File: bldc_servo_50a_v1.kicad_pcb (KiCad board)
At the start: 2 copper layers, 101 parts, among them IC1 DRV8305NQPHPRQ1, J1 CAN_JST-1, J2 CAN_JST-2, J4 Fan_JST, J5 SWD, Q1 BSC010N04LS, Q2 BSC010N04LS, Q3 BSC010N04LS, Q4 BSC010N04LS, Q5 BSC010N04LS, Q6 BSC010N04LS, U1 TLV75533PDBV, U2 SN65HVD230, U3 LMR51430, U4 TPS2051BDBV, U5 STM32G431CBT6

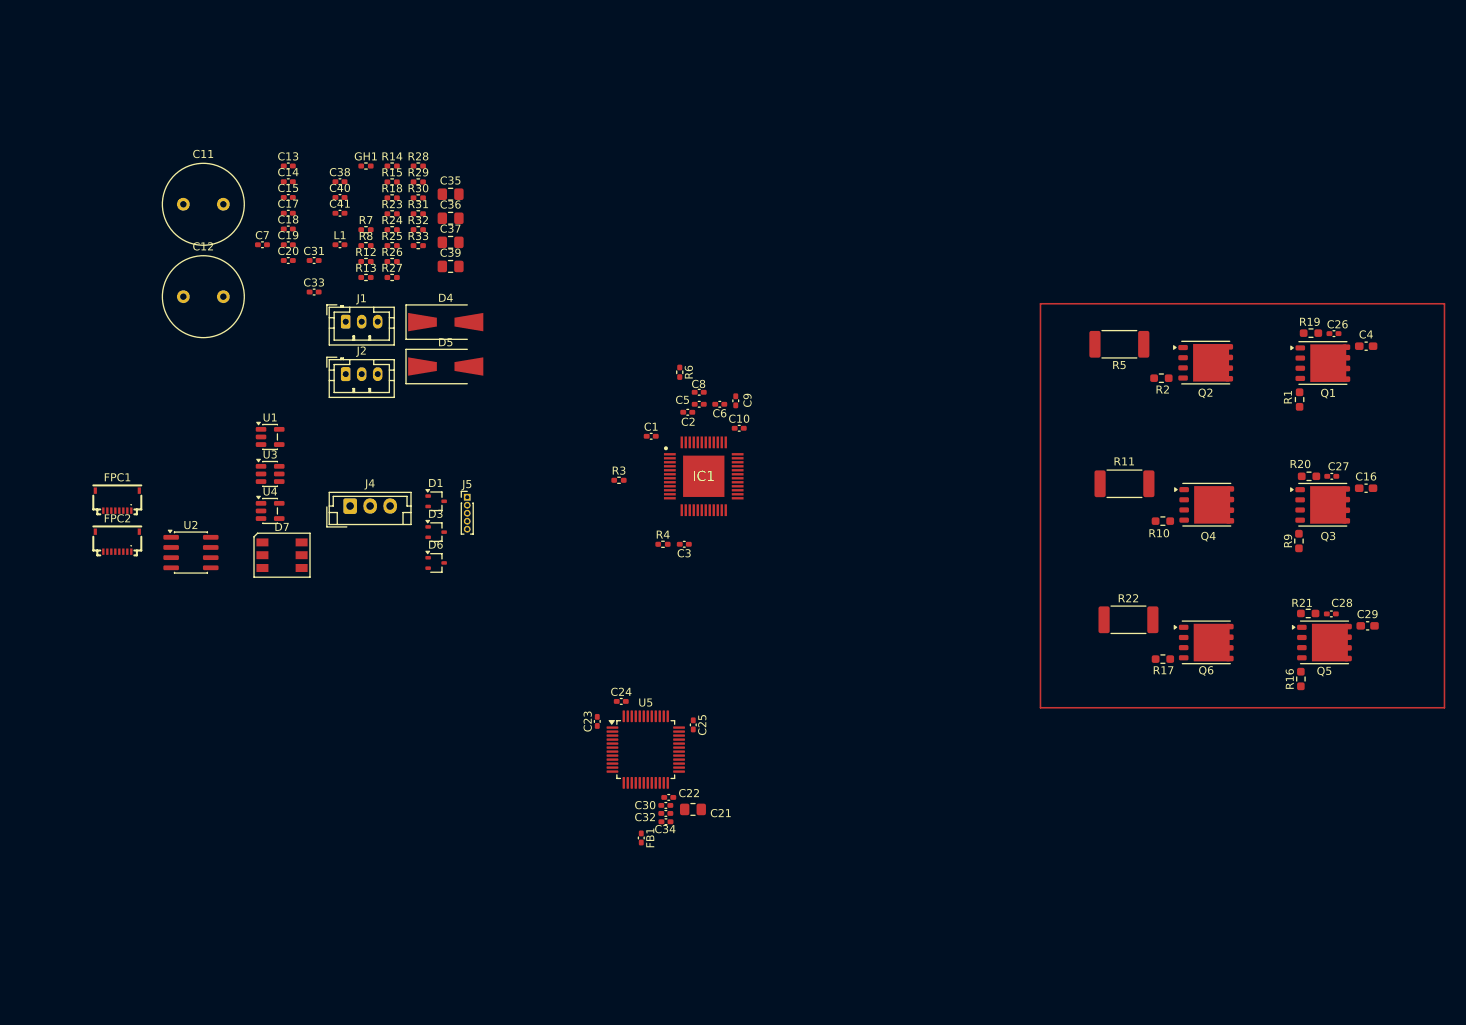
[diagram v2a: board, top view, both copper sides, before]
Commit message: Removed duplicate V_Sensing
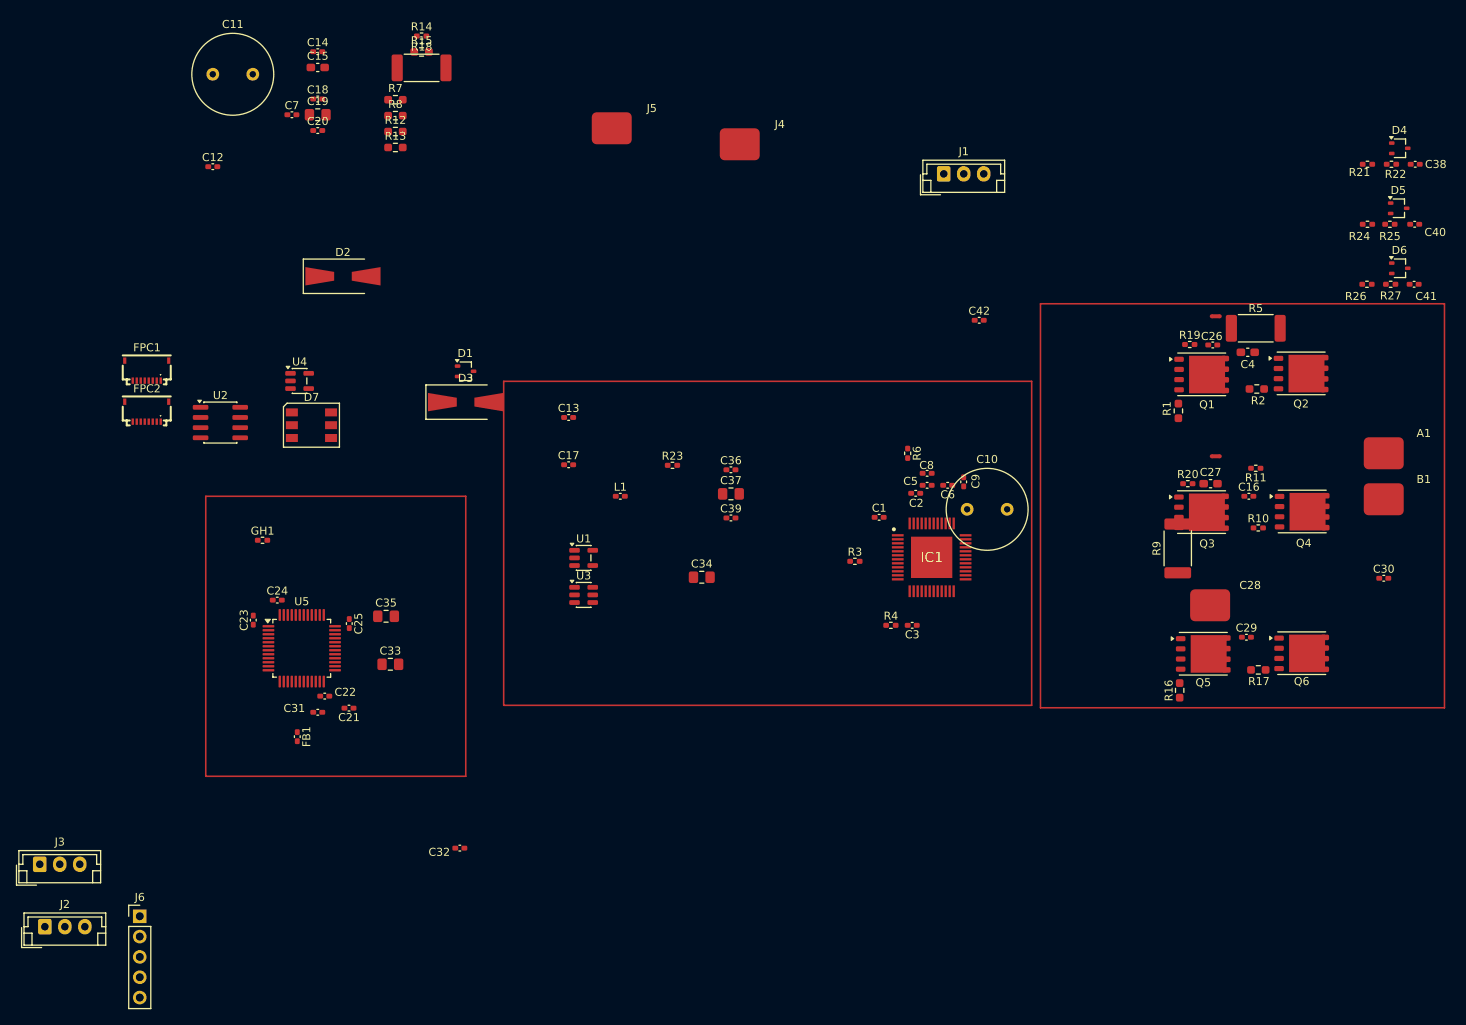
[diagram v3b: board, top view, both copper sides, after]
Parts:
- removed R28, R31, R33: 5k, Resistor_SMD:R_0402_1005Metric_Pad0.72x0.64mm_HandSolder
- removed R29: 10k1, Resistor_SMD:R_0402_1005Metric_Pad0.72x0.64mm_HandSolder
- removed R30, R32: 34.8k, Resistor_SMD:R_0402_1005Metric_Pad0.72x0.64mm_HandSolder
- added A1: A, Solder_Pads:Solder_Pad_5mmx4mm, F.Cu at (224.5, 58.6)
- added B1: B, Solder_Pads:Solder_Pad_5mmx4mm, F.Cu at (224.5, 64.4)
- added C42: 100n, Capacitor_SMD:C_0402_1005Metric_Pad0.74x0.62mm_HandSolder, F.Cu at (173.9, 39.5)
- added D2: SMAJ440A_TVS, Diode_SMD:D_SMA-SMB_Universal_Handsoldering, F.Cu at (94.4, 34.0)
- added J3: Fan_JST, Connector_JST:JST_EH_B3B-EH-A_1x03_P2.50mm_Vertical, F.Cu at (56.5, 107.5)
- added J6: SWD, Connector_PinHeader_2.54mm:PinHeader_1x05_P2.54mm_Vertical, F.Cu at (69.0, 114.0)
- added NT1: NetTie_2, NetTie:NetTie-2_SMD_Pad0.5mm, F.Cu at (203.5, 39.0)
- added NT2: NetTie_2, NetTie:NetTie-2_SMD_Pad0.5mm, F.Cu at (203.5, 56.5)
- added NT3: NetTie_2, NetTie:NetTie-2_SMD_Pad0.5mm, F.Cu at (203.5, 74.5)
- C10: value 1u -> 470u; footprint Capacitor_SMD:C_0402_1005Metric_Pad0.74x0.62mm_HandSolder -> Capacitor_THT:C_Radial_D10.0mm_H16.0mm_P5.00mm
- C12: value 470u -> 1u; footprint Capacitor_THT:C_Radial_D10.0mm_H16.0mm_P5.00mm -> Capacitor_SMD:C_0402_1005Metric_Pad0.74x0.62mm_HandSolder
- C13: value 1u -> 0.1u
- C14: value 0.1u -> 0.01u
- C15: value 0.01u -> 1u; footprint Capacitor_SMD:C_0402_1005Metric_Pad0.74x0.62mm_HandSolder -> Capacitor_SMD:C_0603_1608Metric_Pad1.08x0.95mm_HandSolder
- C16: footprint Capacitor_SMD:C_0603_1608Metric_Pad1.08x0.95mm_HandSolder -> Capacitor_SMD:C_0402_1005Metric_Pad0.74x0.62mm_HandSolder
- C18, C31, C32: value 1u -> 100n
- C19: value 1u -> 10u; footprint Capacitor_SMD:C_0402_1005Metric_Pad0.74x0.62mm_HandSolder -> Capacitor_SMD:C_0805_2012Metric_Pad1.18x1.45mm_HandSolder
- C21, C36, C39: value 10u -> 100n; footprint Capacitor_SMD:C_0805_2012Metric_Pad1.18x1.45mm_HandSolder -> Capacitor_SMD:C_0402_1005Metric_Pad0.74x0.62mm_HandSolder
- C24, C25: value 100n -> 22n
- C27: value 22n -> 1u; footprint Capacitor_SMD:C_0402_1005Metric_Pad0.74x0.62mm_HandSolder -> Capacitor_SMD:C_0603_1608Metric_Pad1.08x0.95mm_HandSolder
- C28: value 22n -> C; footprint Capacitor_SMD:C_0402_1005Metric_Pad0.74x0.62mm_HandSolder -> Solder_Pads:Solder_Pad_5mmx4mm
- C29: value 1u -> 10n; footprint Capacitor_SMD:C_0603_1608Metric_Pad1.08x0.95mm_HandSolder -> Capacitor_SMD:C_0402_1005Metric_Pad0.74x0.62mm_HandSolder
- C30: value 10n -> 1u
- C33, C34: value 100n -> 10u; footprint Capacitor_SMD:C_0402_1005Metric_Pad0.74x0.62mm_HandSolder -> Capacitor_SMD:C_0805_2012Metric_Pad1.18x1.45mm_HandSolder
- C38, C40, C41: value 100n -> 1u
- C7: value 1u -> 4.7u
- C8: value 4.7u -> 2.2u
- C9: value 2.2u -> 1u
- D1: value BAT54SW -> D_Schottky
- D3: value BAT54SW -> SMAJ440A_TVS; footprint Package_TO_SOT_SMD:SOT-323_SC-70 -> Diode_SMD:D_SMA-SMB_Universal_Handsoldering
- D4, D5: value SMAJ440A_TVS -> BAT54SW; footprint Diode_SMD:D_SMA-SMB_Universal_Handsoldering -> Package_TO_SOT_SMD:SOT-323_SC-70
- J1, J2: footprint Connector_JST:JST_PH_B3B-PH-K_1x03_P2.00mm_Vertical -> Connector_JST:JST_EH_B3B-EH-A_1x03_P2.50mm_Vertical
- J4: value Fan_JST -> PVDD; footprint Connector_JST:JST_EH_B3B-EH-A_1x03_P2.50mm_Vertical -> Solder_Pads:Solder_Pad_5mmx4mm
- J5: value SWD -> GND; footprint Connector_PinHeader_1.00mm:PinHeader_1x05_P1.00mm_Vertical -> Solder_Pads:Solder_Pad_5mmx4mm
- R10, R21: value 10 -> 34.8k; footprint Resistor_SMD:R_0603_1608Metric_Pad0.98x0.95mm_HandSolder -> Resistor_SMD:R_0402_1005Metric_Pad0.72x0.64mm_HandSolder
- R11, R22: value 1m -> 5k; footprint Resistor_SMD:R_2512_6332Metric_Pad1.40x3.35mm_HandSolder -> Resistor_SMD:R_0402_1005Metric_Pad0.72x0.64mm_HandSolder
- R12, R7: value 34.8k -> 10; footprint Resistor_SMD:R_0402_1005Metric_Pad0.72x0.64mm_HandSolder -> Resistor_SMD:R_0603_1608Metric_Pad0.98x0.95mm_HandSolder
- R13, R15, R8: value 5k -> 10; footprint Resistor_SMD:R_0402_1005Metric_Pad0.72x0.64mm_HandSolder -> Resistor_SMD:R_0603_1608Metric_Pad0.98x0.95mm_HandSolder
- R14: value 34.8k -> 120
- R18: value 120 -> 1m; footprint Resistor_SMD:R_0402_1005Metric_Pad0.72x0.64mm_HandSolder -> Resistor_SMD:R_2512_6332Metric_Pad1.40x3.35mm_HandSolder
- R19: value 10 -> 100k; footprint Resistor_SMD:R_0603_1608Metric_Pad0.98x0.95mm_HandSolder -> Resistor_SMD:R_0402_1005Metric_Pad0.72x0.64mm_HandSolder
- R20: value 10 -> 13.7k; footprint Resistor_SMD:R_0603_1608Metric_Pad0.98x0.95mm_HandSolder -> Resistor_SMD:R_0402_1005Metric_Pad0.72x0.64mm_HandSolder
- R23: value 100k -> 10k1
- R24: value 13.7k -> 34.8k
- R25, R27: value 34.8k -> 5k
- R26: value 5k -> 34.8k
- R9: value 10 -> 1m; footprint Resistor_SMD:R_0603_1608Metric_Pad0.98x0.95mm_HandSolder -> Resistor_SMD:R_2512_6332Metric_Pad1.40x3.35mm_HandSolder
- moved C41 134.6 mm to (228.3, 35.0)
- moved C38 134.4 mm to (228.4, 20.0)
- moved C40 134.4 mm to (228.4, 27.5)
- moved D6 126.0 mm to (226.5, 33.0)
- moved R27 124.8 mm to (225.4, 35.0)
- moved R25 124.7 mm to (225.3, 27.5)
- moved R24 121.9 mm to (222.5, 27.5)
- moved R26 121.9 mm to (222.4, 35.0)
- moved D4 121.2 mm to (226.5, 18.0)
- moved D5 120.8 mm to (226.4, 25.5)
- moved C30 94.1 mm to (224.5, 71.8)
- moved J2 78.6 mm to (57.1, 115.3)
- moved J1 77.0 mm to (169.5, 21.2)
- moved R22 65.7 mm to (225.5, 20.0), turned to 0 degrees
- moved J4 64.8 mm to (144.0, 20.0)
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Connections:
- C10 pad 1: Net-(IC1-VCP_LSD) -> PVDD
- C12 pad 1: PVDD -> +5V
- C12 pad 2: GND -> Net-(U1-GND)
- C13 pad 1: +5V -> PVDD
- C13 pad 2: Net-(U1-GND) -> GND
- C16 pad 1: PVDD -> +3.3V
- C16 pad 2: GND -> Net-(U1-GND)
- C17 pad 1: +3.3V -> /PVDDSENSE
- C17 pad 2: Net-(U1-GND) -> GND
- C18 pad 1: /BSENSE -> +3.3V
- C19 pad 1: /PVDDSENSE -> +3.3V
- C24 pad 1: +3.3V -> /R_C_PhaseA
- C24 pad 2: GND -> PVDD
- C25 pad 1: +3.3V -> /R_C_PhaseB
- C25 pad 2: GND -> PVDD
- C26 pad 1: /R_C_PhaseA -> /R_C_PhaseC
- C27 pad 1: /R_C_PhaseB -> PVDD
- C27 pad 2: PVDD -> GND
- C28 pad 1: /R_C_PhaseC -> /PHASE_C
- C29 pad 1: PVDD -> +3.3VA
- C31 pad 1: /CSENSE -> /5V_SW
- C31 pad 2: GND -> /5V_BOOT
- C33 pad 1: /5V_SW -> +5V
- C33 pad 2: /5V_BOOT -> GND
- C34 pad 1: +3.3VA -> PVDD
- C38 pad 1: PVDD -> Net-(D4-COM)
- C39 pad 1: +5V -> /NRST
- C40 pad 1: /NRST -> Net-(D5-COM)
- C41 pad 1: GND -> Net-(D6-COM)
- C41 pad 2: +5V -> GND
- C7 pad 1: /ASENSE -> PVDD
- C8 pad 1: PVDD -> Net-(IC1-VCPH)
- C8 pad 2: GND -> PVDD
- C9 pad 1: Net-(IC1-VCPH) -> Net-(IC1-VCP_LSD)
- C9 pad 2: PVDD -> GND
- D1 pad 1: GND -> +3.3V
- D1 pad 2: +3V3 -> /PVDDSENSE
- D1 pad 3: /ASENSE -> (no net)
- D3 pad 1: GND -> /CAN_L
- D3 pad 2: +3V3 -> GND
- D4 pad 1: /CAN_H -> GND
- D4 pad 2: GND -> +3V3
- D5 pad 1: /CAN_L -> GND
- D5 pad 2: GND -> +3V3
- D6 pad 3: /CSENSE -> Net-(D6-COM)
- IC1 pad 20: GND -> /SP3
- IC1 pad 22: GND -> /SP2
- IC1 pad 23: /SN1 -> /SL_A
- J4 pad 1: /FAN -> PVDD
- J5 pad 1: +3.3V -> GND
- R10 pad 1: /GL_B -> PVDD
- R10 pad 2: Net-(Q4-G) -> /PVDDSENSE
- R11 pad 1: /SL_B -> /PVDDSENSE
- R12 pad 1: PVDD -> /GH_C
- R12 pad 2: /PVDDSENSE -> Net-(Q5-G)
- R13 pad 1: /PVDDSENSE -> /GL_C
- R13 pad 2: GND -> Net-(Q6-G)
- R14 pad 1: /PHASE_B -> Net-(JP1-A)
- R14 pad 2: /BSENSE -> /CAN_L
- R15 pad 1: /BSENSE -> /PHASE_A
- R15 pad 2: GND -> /R_C_PhaseA
- R16 pad 1: /GH_C -> /PHASE_B
- R16 pad 2: Net-(Q5-G) -> /R_C_PhaseB
- R17 pad 1: /GL_C -> /PHASE_C
- R17 pad 2: Net-(Q6-G) -> /R_C_PhaseC
- R18 pad 1: Net-(JP1-A) -> /SL_C
- R18 pad 2: /CAN_L -> /SP3
- R19 pad 1: /PHASE_A -> +5V
- R19 pad 2: /R_C_PhaseA -> /5V_FB
- R20 pad 1: /PHASE_B -> /5V_FB
- R20 pad 2: /R_C_PhaseB -> GND
- R21 pad 1: /PHASE_C -> /PHASE_A
- R21 pad 2: /R_C_PhaseC -> /SH_A_SENSE
- R22 pad 1: /SL_C -> /SH_A_SENSE
- R23 pad 1: +5V -> +3V3
- R23 pad 2: /5V_FB -> /TEMP
- R24 pad 1: /5V_FB -> /PHASE_B
- R24 pad 2: GND -> /SH_B_SENSE
- R25 pad 1: /PHASE_C -> /SH_B_SENSE
- R25 pad 2: /CSENSE -> GND
- R26 pad 1: /CSENSE -> /PHASE_C
- R26 pad 2: GND -> /SH_C_SENSE
- R27 pad 1: /PHASE_A -> /SH_C_SENSE
- R27 pad 2: /SH_A_SENSE -> GND
- R5 pad 2: GND -> /SP1
- R7 pad 1: /PHASE_A -> /GH_B
- R7 pad 2: /ASENSE -> Net-(Q3-G)
- R8 pad 1: /ASENSE -> /GL_B
- R8 pad 2: GND -> Net-(Q4-G)
- R9 pad 1: /GH_B -> /SL_B
- R9 pad 2: Net-(Q3-G) -> /SP2

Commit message: Structure for PCB, tentative
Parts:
- moved C30 145.9 mm to (82.5, 38.1)
- moved R18 124.6 mm to (208.9, 75.5), turned to 180 degrees
- moved C29 118.7 mm to (93.9, 44.1)
- moved C24 112.5 mm to (194.9, 45.5)
- moved C15 104.0 mm to (191.8, 34.6)
- moved C25 101.0 mm to (195.2, 63.0), turned to 0 degrees
- moved R15 99.5 mm to (194.9, 47.0), turned to 180 degrees
- moved J1 93.9 mm to (90.2, 71.6)
- moved R12 88.8 mm to (187.1, 37.5)
- moved R13 88.8 mm to (187.1, 39.5)
- moved R7 88.8 mm to (187.1, 33.5)
- moved R8 88.8 mm to (187.1, 35.5)
- moved C16 88.1 mm to (122.7, 38.1)
- moved C7 86.5 mm to (168.7, 45.1), turned to 180 degrees
- moved C11 79.6 mm to (156.7, 21.1)
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
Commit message: Wip: before fixing footprints
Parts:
- moved C11 40.5 mm to (173.5, 58.0)
- moved C10 37.9 mm to (184.5, 58.0)
- moved J4 11.9 mm to (166.5, 91.1)
- moved J5 11.9 mm to (173.5, 91.1)
- moved NT3 9.96 mm to (213.0, 71.5), turned to 90 degrees
- moved R17 9.78 mm to (187.9, 76.6)
- moved C26 9.78 mm to (187.7, 75.1)
- moved Q5 9.78 mm to (193.8, 75.8)
- moved FPC1 9.78 mm to (77.0, 90.5), turned to 180 degrees
- moved Q6 9.54 mm to (206.8, 75.1)
- moved R18 7.05 mm to (216.0, 75.5)
- moved C13 6.46 mm to (143.1, 22.0)
- moved C14 6.46 mm to (143.1, 23.0)
- moved C17 6.46 mm to (145.5, 23.0)
- moved D1 6.46 mm to (144.1, 27.5)
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
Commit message: Schematic done
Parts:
- removed A1: A, Solder_Pads:Solder_Pad_5mmx4mm
- removed B1: B, Solder_Pads:Solder_Pad_5mmx4mm
- removed D7: WS2812, LED_SMD:LED_WS2812_PLCC6_5.0x5.0mm_P1.6mm
- removed GH1: 10k, Resistor_SMD:R_0402_1005Metric_Pad0.72x0.64mm_HandSolder
- removed IC1: DRV8305NQPHPRQ1, DRV8305NQPHPRQ1:QFP50P900X900X120-49N
- removed J6: SWD, Connector_PinHeader_2.54mm:PinHeader_1x05_P2.54mm_Vertical
- added C43: 100n, Capacitor_SMD:C_0402_1005Metric_Pad0.74x0.62mm_HandSolder, F.Cu at (156.4, 30.0)
- added C44: 1u, Capacitor_SMD:C_0603_1608Metric_Pad1.08x0.95mm_HandSolder, F.Cu at (115.1, 18.6)
- added C45: 1u, Capacitor_SMD:C_0603_1608Metric_Pad1.08x0.95mm_HandSolder, F.Cu at (115.1, 21.1)
- added C46: 100n, Capacitor_SMD:C_0402_1005Metric_Pad0.74x0.62mm_HandSolder, F.Cu at (85.2, 97.9)
- added C47: 100n, Capacitor_SMD:C_0402_1005Metric_Pad0.74x0.62mm_HandSolder, F.Cu at (162.4, -9.00)
- added C48: 100n, Capacitor_SMD:C_0402_1005Metric_Pad0.74x0.62mm_HandSolder, F.Cu at (50.9, 167.9)
- added C49: 1u, Capacitor_SMD:C_0603_1608Metric_Pad1.08x0.95mm_HandSolder, F.Cu at (43.7, 125.4)
- added C50: 1n, Capacitor_SMD:C_0603_1608Metric_Pad1.08x0.95mm_HandSolder, F.Cu at (226.6, 81.5)
- added C51: 1n, Capacitor_SMD:C_0603_1608Metric_Pad1.08x0.95mm_HandSolder, F.Cu at (243.8, 111.6)
- added C52: 1n, Capacitor_SMD:C_0603_1608Metric_Pad1.08x0.95mm_HandSolder, F.Cu at (269.4, 143.7)
- added C53: 1u, Capacitor_SMD:C_0603_1608Metric_Pad1.08x0.95mm_HandSolder, F.Cu at (73.6, 175.5)
- added C54: 1n, Capacitor_SMD:C_0402_1005Metric_Pad0.74x0.62mm_HandSolder, F.Cu at (229.9, 104.0)
- added C55: 1n, Capacitor_SMD:C_0402_1005Metric_Pad0.74x0.62mm_HandSolder, F.Cu at (255.9, 135.5)
- added C56: 1n, Capacitor_SMD:C_0402_1005Metric_Pad0.74x0.62mm_HandSolder, F.Cu at (281.4, 167.5)
- added H1: ~, positive_altitude:Positive_Altitude_M2_Hole, F.Cu at (167.5, 175.8)
- added H2: ~, positive_altitude:Positive_Altitude_M2_Hole, F.Cu at (167.5, 181.0)
- added H3: ~, positive_altitude:Positive_Altitude_M2_Hole, F.Cu at (167.5, 186.2)
- added JP1: Enable_CAN_Termination_1, Jumper:SolderJumper-2_P1.3mm_Open_RoundedPad1.0x1.5mm, F.Cu at (85.2, 101.4)
- added NT10: NetTie_2, positive_altitude:NetTie-2_SMD_Pad0.2mm, F.Cu at (281.8, 157.0)
- added NT11: NetTie_2, positive_altitude:NetTie-2_SMD_Pad0.2mm, F.Cu at (281.8, 158.5)
- added NT12: NetTie_2, positive_altitude:NetTie-2_SMD_Pad0.2mm, F.Cu at (281.8, 160.0)
- added NT4: NetTie_2, positive_altitude:NetTie-2_SMD_Pad0.2mm, F.Cu at (236.4, 94.0)
- added NT5: NetTie_2, positive_altitude:NetTie-2_SMD_Pad0.2mm, F.Cu at (238.9, 127.6)
- added NT6: NetTie_2, positive_altitude:NetTie-2_SMD_Pad0.2mm, F.Cu at (238.9, 129.1)
- added NT7: NetTie_2, positive_altitude:NetTie-2_SMD_Pad0.2mm, F.Cu at (240.5, 126.1)
- added NT8: NetTie_2, positive_altitude:NetTie-2_SMD_Pad0.2mm, F.Cu at (240.5, 127.6)
- added NT9: NetTie_2, positive_altitude:NetTie-2_SMD_Pad0.2mm, F.Cu at (279.3, 158.5)
- added P1: PVDD, positive_altitude:Soldering_Pad_8mm_3mm_hole, F.Cu at (144.5, 157.7)
- added P2: GND, positive_altitude:Soldering_Pad_8mm_3mm_hole, F.Cu at (144.5, 166.7)
- added P3: PHASE_A, positive_altitude:Soldering_Pad_8mm_3mm_hole, F.Cu at (287.5, 105.5)
- added P4: PHASE_B, positive_altitude:Soldering_Pad_8mm_3mm_hole, F.Cu at (287.0, 115.5)
- added P5: PHASE_C, positive_altitude:Soldering_Pad_8mm_3mm_hole, F.Cu at (287.0, 124.5)
- added R28: 10k, Resistor_SMD:R_0402_1005Metric_Pad0.72x0.64mm_HandSolder, F.Cu at (73.2, 178.4)
- added TH1: NCP15XH103F03RC, Resistor_SMD:R_0402_1005Metric_Pad0.72x0.64mm_HandSolder, F.Cu at (73.2, 180.4)
- added U6: TPS22919DCKR, TPS22919DCKR:SOT65P210X110-6N, F.Cu at (166.4, -10.8)
- C1, C2, C3: value 1u -> 100u; footprint Capacitor_SMD:C_0402_1005Metric_Pad0.74x0.62mm_HandSolder -> Capacitor_SMD:CP_Elec_10x7.9
- C10, C11: value 470u -> 4.7u; footprint Capacitor_THT:C_Radial_D10.0mm_H16.0mm_P5.00mm -> Capacitor_SMD:C_1206_3216Metric_Pad1.33x1.80mm_HandSolder
- C12, C38, C9: value 1u -> 4.7u; footprint Capacitor_SMD:C_0402_1005Metric_Pad0.74x0.62mm_HandSolder -> Capacitor_SMD:C_1206_3216Metric_Pad1.33x1.80mm_HandSolder
- C13: value 0.1u -> 4.7u; footprint Capacitor_SMD:C_0402_1005Metric_Pad0.74x0.62mm_HandSolder -> Capacitor_SMD:C_1206_3216Metric_Pad1.33x1.80mm_HandSolder
- C14: value 0.01u -> 4.7u; footprint Capacitor_SMD:C_0402_1005Metric_Pad0.74x0.62mm_HandSolder -> Capacitor_SMD:C_1206_3216Metric_Pad1.33x1.80mm_HandSolder
- C16, C17: footprint Capacitor_SMD:C_0402_1005Metric_Pad0.74x0.62mm_HandSolder -> Capacitor_SMD:C_0603_1608Metric_Pad1.08x0.95mm_HandSolder
- C18, C20, C36: value 100n -> 1u; footprint Capacitor_SMD:C_0402_1005Metric_Pad0.74x0.62mm_HandSolder -> Capacitor_SMD:C_0603_1608Metric_Pad1.08x0.95mm_HandSolder
- C19, C34, C35, C37: value 10u -> 1u; footprint Capacitor_SMD:C_0805_2012Metric_Pad1.18x1.45mm_HandSolder -> Capacitor_SMD:C_0603_1608Metric_Pad1.08x0.95mm_HandSolder
- C21: value 100n -> 4.7u; footprint Capacitor_SMD:C_0402_1005Metric_Pad0.74x0.62mm_HandSolder -> Capacitor_SMD:C_0603_1608Metric_Pad1.08x0.95mm_HandSolder
- C24, C25: value 22n -> 100n
- C26: value 22n -> 1u; footprint Capacitor_SMD:C_0402_1005Metric_Pad0.74x0.62mm_HandSolder -> Capacitor_SMD:C_0603_1608Metric_Pad1.08x0.95mm_HandSolder
- C27: value 1u -> 100n; footprint Capacitor_SMD:C_0603_1608Metric_Pad1.08x0.95mm_HandSolder -> Capacitor_SMD:C_0402_1005Metric_Pad0.74x0.62mm_HandSolder
- C28: value C -> 10n; footprint Solder_Pads:Solder_Pad_5mmx4mm -> Capacitor_SMD:C_0402_1005Metric_Pad0.74x0.62mm_HandSolder
- C29: value 10n -> 100n
- C30: value 1u -> 2.2u; footprint Capacitor_SMD:C_0402_1005Metric_Pad0.74x0.62mm_HandSolder -> Capacitor_SMD:C_0603_1608Metric_Pad1.08x0.95mm_HandSolder
- C31, C32: value 100n -> 47n; footprint Capacitor_SMD:C_0402_1005Metric_Pad0.74x0.62mm_HandSolder -> Capacitor_SMD:C_0805_2012Metric_Pad1.18x1.45mm_HandSolder
- C33: value 10u -> 4.7u; footprint Capacitor_SMD:C_0805_2012Metric_Pad1.18x1.45mm_HandSolder -> Capacitor_SMD:C_1206_3216Metric_Pad1.33x1.80mm_HandSolder
- C39: value 100n -> 4.7u; footprint Capacitor_SMD:C_0402_1005Metric_Pad0.74x0.62mm_HandSolder -> Capacitor_SMD:C_1206_3216Metric_Pad1.33x1.80mm_HandSolder
- C4: value 1u -> 100u; footprint Capacitor_SMD:C_0603_1608Metric_Pad1.08x0.95mm_HandSolder -> Capacitor_SMD:CP_Elec_10x7.9
- C40: value 1u -> 100n
- C41: value 1u -> 22u; footprint Capacitor_SMD:C_0402_1005Metric_Pad0.74x0.62mm_HandSolder -> Capacitor_SMD:C_0805_2012Metric_Pad1.18x1.45mm_HandSolder
- C42: value 100n -> 22u; footprint Capacitor_SMD:C_0402_1005Metric_Pad0.74x0.62mm_HandSolder -> Capacitor_SMD:C_0805_2012Metric_Pad1.18x1.45mm_HandSolder
- C5, C6: value 0.047u -> 100u; footprint Capacitor_SMD:C_0402_1005Metric_Pad0.74x0.62mm_HandSolder -> Capacitor_SMD:CP_Elec_10x7.9
- C7: footprint Capacitor_SMD:C_0402_1005Metric_Pad0.74x0.62mm_HandSolder -> Capacitor_SMD:C_1206_3216Metric_Pad1.33x1.80mm_HandSolder
- C8: value 2.2u -> 4.7u; footprint Capacitor_SMD:C_0402_1005Metric_Pad0.74x0.62mm_HandSolder -> Capacitor_SMD:C_1206_3216Metric_Pad1.33x1.80mm_HandSolder
- D1: value D_Schottky -> WS2812B-2020; footprint Package_TO_SOT_SMD:SOT-323_SC-70 -> LED_SMD:LED_WS2812B-2020_PLCC4_2.0x2.0mm
- D2: value SMAJ440A_TVS -> SMBJ28A; footprint Diode_SMD:D_SMA-SMB_Universal_Handsoldering -> Diode_SMD:D_SMB_Handsoldering
- D3: value SMAJ440A_TVS -> BAT54SW; footprint Diode_SMD:D_SMA-SMB_Universal_Handsoldering -> Package_TO_SOT_SMD:SOT-323_SC-70
- FB1: value FB -> BLM15AG601SN1D; footprint Capacitor_SMD:C_0402_1005Metric_Pad0.74x0.62mm_HandSolder -> Resistor_SMD:R_0402_1005Metric_Pad0.72x0.64mm_HandSolder
- FPC1: value External sensor -> Encoder1; footprint HCTL HC-FPC-05-09-8RLTAG_8pin connector:FPC-SMD_8P-P0.50_HC-FPC-05-09-8RLTAG -> HCTL HC-FPC-05-09-8RLTAG:FPC-SMD_8P-P0.50_HC-FPC-05-09-8RLTAG
- FPC2: value External sensor -> Encoder2; footprint HCTL HC-FPC-05-09-8RLTAG_8pin connector:FPC-SMD_8P-P0.50_HC-FPC-05-09-8RLTAG -> HCTL HC-FPC-05-09-8RLTAG:FPC-SMD_8P-P0.50_HC-FPC-05-09-8RLTAG
- J1: value CAN_JST-1 -> CAN1; footprint Connector_JST:JST_EH_B3B-EH-A_1x03_P2.50mm_Vertical -> Connector_JST:JST_PH_S3B-PH-SM4-TB_1x03-1MP_P2.00mm_Horizontal
- J2: value CAN_JST-2 -> CAN2; footprint Connector_JST:JST_EH_B3B-EH-A_1x03_P2.50mm_Vertical -> Connector_JST:JST_PH_S3B-PH-SM4-TB_1x03-1MP_P2.00mm_Horizontal
- J3: value Fan_JST -> FAN; footprint Connector_JST:JST_EH_B3B-EH-A_1x03_P2.50mm_Vertical -> Connector_JST:JST_PH_S3B-PH-SM4-TB_1x03-1MP_P2.00mm_Horizontal
- J4: value PVDD -> SWD; footprint Solder_Pads:Solder_Pad_5mmx4mm -> Connector_PinHeader_2.54mm:PinHeader_1x05_P2.54mm_Vertical
- J5: value GND -> SWD; footprint Solder_Pads:Solder_Pad_5mmx4mm -> positive_altitude:Positive_Altitude_SWD_Connector
- L1: value 3.3uH -> 3.3u; footprint Capacitor_SMD:C_0402_1005Metric_Pad0.74x0.62mm_HandSolder -> Inductor_SMD:L_Changjiang_FXL0420
- NT1, NT2, NT3: footprint NetTie:NetTie-2_SMD_Pad0.5mm -> positive_altitude:NetTie-2_SMD_Pad0.2mm
- R1, R2: value 10 -> 1m; footprint Resistor_SMD:R_0603_1608Metric_Pad0.98x0.95mm_HandSolder -> Resistor_SMD:R_2512_6332Metric_Pad1.40x3.35mm_HandSolder
- R10: value 34.8k -> 100
- R11: value 5k -> 220
- R12, R13: value 10 -> 10k; footprint Resistor_SMD:R_0603_1608Metric_Pad0.98x0.95mm_HandSolder -> Resistor_SMD:R_0402_1005Metric_Pad0.72x0.64mm_HandSolder
- R14: value 120 -> 100k
- R15: value 10 -> 13.7k; footprint Resistor_SMD:R_0603_1608Metric_Pad0.98x0.95mm_HandSolder -> Resistor_SMD:R_0402_1005Metric_Pad0.72x0.64mm_HandSolder
- R16: value 10 -> 120; footprint Resistor_SMD:R_0603_1608Metric_Pad0.98x0.95mm_HandSolder -> Resistor_SMD:R_0402_1005Metric_Pad0.72x0.64mm_HandSolder
- R17: value 10 -> 39k; footprint Resistor_SMD:R_0603_1608Metric_Pad0.98x0.95mm_HandSolder -> Resistor_SMD:R_0402_1005Metric_Pad0.72x0.64mm_HandSolder
- R18: value 1m -> 39k; footprint Resistor_SMD:R_2512_6332Metric_Pad1.40x3.35mm_HandSolder -> Resistor_SMD:R_0402_1005Metric_Pad0.72x0.64mm_HandSolder
- R19: value 100k -> 39k
- R20: value 13.7k -> 39k
- R21, R24: value 34.8k -> 5k
- R23: value 10k1 -> 5k
- R25, R27: value 5k -> 10; footprint Resistor_SMD:R_0402_1005Metric_Pad0.72x0.64mm_HandSolder -> Resistor_SMD:R_0603_1608Metric_Pad0.98x0.95mm_HandSolder
- R26: value 34.8k -> 10; footprint Resistor_SMD:R_0402_1005Metric_Pad0.72x0.64mm_HandSolder -> Resistor_SMD:R_0603_1608Metric_Pad0.98x0.95mm_HandSolder
- R3: value 10k -> 1m; footprint Resistor_SMD:R_0402_1005Metric_Pad0.72x0.64mm_HandSolder -> Resistor_SMD:R_2512_6332Metric_Pad1.40x3.35mm_HandSolder
- R4: value 10k -> 2.2; footprint Resistor_SMD:R_0402_1005Metric_Pad0.72x0.64mm_HandSolder -> Resistor_SMD:R_0603_1608Metric_Pad0.98x0.95mm_HandSolder
- R5, R9: value 1m -> 2.2; footprint Resistor_SMD:R_2512_6332Metric_Pad1.40x3.35mm_HandSolder -> Resistor_SMD:R_0603_1608Metric_Pad0.98x0.95mm_HandSolder
- R6: value 100 -> 2.2; footprint Resistor_SMD:R_0402_1005Metric_Pad0.72x0.64mm_HandSolder -> Resistor_SMD:R_0603_1608Metric_Pad0.98x0.95mm_HandSolder
- R7, R8: value 10 -> 2.2
- U1: value TLV75533PDBV -> STM32G431CBT6; footprint Package_TO_SOT_SMD:SOT-23-5 -> Package_QFP:LQFP-48_7x7mm_P0.5mm
- U2: value SN65HVD230 -> DRV8305NQPHPRQ1; footprint Package_SO:SOIC-8_3.9x4.9mm_P1.27mm -> DRV8305NQPHPRQ1:QFP50P900X900X120-49N
- U4: value TPS2051BDBV -> TLV75533PDBV
- U5: value STM32G431CBT6 -> SN65HVD230; footprint Package_QFP:LQFP-48_7x7mm_P0.5mm -> Package_SO:SOIC-8_3.9x4.9mm_P1.27mm
- moved D4 206.8 mm to (39.2, 133.9)
- moved C20 205.6 mm to (276.8, 147.2)
- moved D5 204.6 mm to (39.2, 137.6)
- moved C19 203.7 mm to (276.8, 144.7)
- moved R22 203.6 mm to (45.2, 140.4)
- moved D6 202.6 mm to (39.2, 141.3)
- moved R21 200.0 mm to (45.2, 138.4)
- moved R24 188.5 mm to (48.5, 130.5)
- moved R19 180.3 mm to (45.2, 134.5)
- moved R18 180.0 mm to (45.2, 132.5), turned to 0 degrees
- moved R20 172.7 mm to (45.2, 136.5)
- moved D1 165.5 mm to (50.9, 164.2)
- moved C18 164.9 mm to (250.3, 117.6)
- moved C28 161.5 mm to (81.6, 145.7)
- moved R3 157.7 mm to (272.4, 167.0)
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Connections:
- C1 pad 1: +3.3V -> PVDD
- C1 pad 2: Net-(IC1-VREG) -> GND
- C10 pad 1: PVDD -> GND
- C10 pad 2: GND -> PVDD
- C11 pad 1: PVDD -> GND
- C11 pad 2: GND -> PVDD
- C12 pad 1: +5V -> GND
- C12 pad 2: Net-(U1-GND) -> PVDD
- C13 pad 1: PVDD -> GND
- C13 pad 2: GND -> PVDD
- C14 pad 1: PVDD -> GND
- C14 pad 2: GND -> PVDD
- C16 pad 1: +3.3V -> PVDD
- C16 pad 2: Net-(U1-GND) -> GND
- C17 pad 1: /PVDDSENSE -> PVDD
- C18 pad 1: +3.3V -> PVDD
- C19 pad 1: +3.3V -> PVDD
- C2 pad 1: GND -> PVDD
- C2 pad 2: Net-(IC1-DVDD) -> GND
- C20 pad 1: +3.3V -> PVDD
- C21 pad 1: +3.3V -> GND
- C21 pad 2: GND -> +3.3V
- C22 pad 1: +3.3V -> GND
- C22 pad 2: GND -> +3.3V
- C23 pad 1: +3.3V -> GND
- C23 pad 2: GND -> +3.3V
- C24 pad 1: /R_C_PhaseA -> GND
- C24 pad 2: PVDD -> +3.3V
- C25 pad 1: /R_C_PhaseB -> GND
- C25 pad 2: PVDD -> +3.3V
- C26 pad 1: /R_C_PhaseC -> +3.3VA
- C26 pad 2: PVDD -> GND
- C27 pad 1: PVDD -> +3.3VA
- C28 pad 1: /PHASE_C -> +3.3VA
- C29 pad 1: +3.3VA -> /NRST
- C3 pad 1: Net-(IC1-AVDD) -> PVDD
- C30 pad 1: +3.3VA -> /DRV_VCPH
- C30 pad 2: GND -> PVDD
- C31 pad 1: /5V_SW -> /DRV_CP1H
- C31 pad 2: /5V_BOOT -> /DRV_CP1L
- C32 pad 1: +3.3VA -> /DRV_CP2H
- C32 pad 2: GND -> /DRV_CP2L
- C33 pad 1: +5V -> PVDD
- C34 pad 1: PVDD -> /DRV_VCP_LSD
- C35 pad 1: +5V -> /DRV_AVDD
- C36 pad 1: PVDD -> /DRV_DVDD
- C37 pad 1: +5V -> /DRV_VREG
- C38 pad 1: Net-(D4-COM) -> PVDD
- C39 pad 1: /NRST -> PVDD
- C40 pad 1: Net-(D5-COM) -> PVDD
- C41 pad 1: Net-(D6-COM) -> +5V
- C42 pad 1: GND -> +5V
- C42 pad 2: +5V -> GND
- C5 pad 1: Net-(IC1-CP1L) -> PVDD
- C5 pad 2: Net-(IC1-CP1H) -> GND
- C6 pad 1: Net-(IC1-CP2H) -> PVDD
- C6 pad 2: Net-(IC1-CP2L) -> GND
- C7 pad 1: PVDD -> GND
- C7 pad 2: GND -> PVDD
- C8 pad 1: Net-(IC1-VCPH) -> GND
- C9 pad 1: Net-(IC1-VCP_LSD) -> GND
- C9 pad 2: GND -> PVDD
- D1 pad 1: +3.3V -> unconnected-(D1-DOUT-Pad1)
- D1 pad 2: /PVDDSENSE -> GND
- D1 pad 3: (no net) -> /LED
- D2 pad 1: /CAN_H -> PVDD
- D3 pad 1: /CAN_L -> GND
- D3 pad 2: GND -> +3.3V
- D4 pad 2: +3V3 -> +3.3V
- D4 pad 3: Net-(D4-COM) -> /PHASE_B_SENSE
- D5 pad 2: +3V3 -> +3.3V
- D5 pad 3: Net-(D5-COM) -> /PHASE_C_SENSE
- D6 pad 2: +3V3 -> +3.3V
- D6 pad 3: Net-(D6-COM) -> /PVDD_SENSE
- J3 pad 1: /FAN -> /FAN_5V
- J3 pad 2: +5V -> GND
- J3 pad 3: GND -> /FAN_PWM
- J4 pad 1: PVDD -> +3.3V
- J5 pad 1: GND -> +3.3V
- L1 pad 1: /5V_SW -> +5V
- L1 pad 2: +5V -> /5V_SW
- NT1 pad 1: /SP1 -> /SL_A
- NT1 pad 2: GND -> Net-(Q2-S_1)
- NT2 pad 1: /SP2 -> /SN1
- NT2 pad 2: GND -> Net-(Q2-S_1)
- NT3 pad 1: /SP3 -> /SH_A
- NT3 pad 2: GND -> /PHASE_A
- Q2 pad 1: /SL_A -> Net-(Q2-S_1)
- Q2 pad 2: /SL_A -> Net-(Q2-S_1)
- Q2 pad 3: /SL_A -> Net-(Q2-S_1)
- Q4 pad 1: /SL_B -> Net-(Q4-S_1)
- Q4 pad 2: /SL_B -> Net-(Q4-S_1)
- Q4 pad 3: /SL_B -> Net-(Q4-S_1)
- Q6 pad 1: /SL_C -> Net-(Q6-S_1)
- Q6 pad 2: /SL_C -> Net-(Q6-S_1)
- Q6 pad 3: /SL_C -> Net-(Q6-S_1)
- R1 pad 1: /GH_A -> Net-(Q2-S_1)
- R1 pad 2: Net-(Q1-G) -> GND
- R10 pad 2: /PVDDSENSE -> /DRV_VDRAIN
- R11 pad 1: /PVDDSENSE -> +3.3V
- R11 pad 2: GND -> /DRV_VREG
- R12 pad 1: /GH_C -> +3.3V
- R12 pad 2: Net-(Q5-G) -> /DRV_NFAULT
- R13 pad 1: /GL_C -> +3.3V
- R13 pad 2: Net-(Q6-G) -> /DRV_PWRGD
- R14 pad 1: Net-(JP1-A) -> +5V
- R14 pad 2: /CAN_L -> /5V_FB
- R15 pad 1: /PHASE_A -> /5V_FB
- R15 pad 2: /R_C_PhaseA -> GND
- R16 pad 1: /PHASE_B -> Net-(JP1-A)
- R16 pad 2: /R_C_PhaseB -> /CAN_L
- R17 pad 1: /PHASE_C -> /PHASE_A
- R17 pad 2: /R_C_PhaseC -> /PHASE_A_SENSE
- R18 pad 1: /SL_C -> /PHASE_B
- R18 pad 2: /SP3 -> /PHASE_B_SENSE
- R19 pad 1: +5V -> /PHASE_C
- R19 pad 2: /5V_FB -> /PHASE_C_SENSE
- R2 pad 1: /GL_A -> Net-(Q4-S_1)
- R2 pad 2: Net-(Q2-G) -> GND
- R20 pad 1: /5V_FB -> PVDD
- R20 pad 2: GND -> /PVDD_SENSE
- R21 pad 1: /PHASE_A -> /PHASE_A_SENSE
- R21 pad 2: /SH_A_SENSE -> GND
- R22 pad 1: /SH_A_SENSE -> /PHASE_B_SENSE
- R23 pad 1: +3V3 -> /PHASE_C_SENSE
- R23 pad 2: /TEMP -> GND
- R24 pad 1: /PHASE_B -> /PVDD_SENSE
- R24 pad 2: /SH_B_SENSE -> GND
- R25 pad 1: /SH_B_SENSE -> /PHASE_A
- R25 pad 2: GND -> /R_C_PhaseA
- R26 pad 1: /PHASE_C -> /PHASE_B
- R26 pad 2: /SH_C_SENSE -> /R_C_PhaseB
- R27 pad 1: /SH_C_SENSE -> /PHASE_C
- R27 pad 2: GND -> /R_C_PhaseC
- R3 pad 1: +3.3V -> Net-(Q6-S_1)
- R3 pad 2: /NFAULT -> GND
- R4 pad 1: +3.3V -> /GH_A
- R4 pad 2: /PWRGD -> Net-(Q1-G)
- R5 pad 1: /SL_A -> /GL_A
- R5 pad 2: /SP1 -> Net-(Q2-G)
- R6 pad 1: PVDD -> /GH_B
- R6 pad 2: Net-(IC1-VDRAIN) -> Net-(Q3-G)
- R7 pad 1: /GH_B -> /GL_B
- R7 pad 2: Net-(Q3-G) -> Net-(Q4-G)
- R8 pad 1: /GL_B -> /GH_C
- R8 pad 2: Net-(Q4-G) -> Net-(Q5-G)
- R9 pad 1: /SL_B -> /GL_C
- R9 pad 2: /SP2 -> Net-(Q6-G)
- U1 pad 1: +5V -> +3.3V
- U1 pad 2: Net-(U1-GND) -> /EN_GATE
- U1 pad 3: +5V -> /DRV_WAKE
- U1 pad 5: +3.3V -> /PVDD_SENSE
- U2 pad 1: /CAN_TX -> /EN_GATE
- U2 pad 2: GND -> /INHA
- U2 pad 3: +3.3V -> /INLA
- U2 pad 4: /CAN_RX -> /INHB
- U2 pad 5: unconnected-(U2-Vref-Pad5) -> /INLB
- U2 pad 6: /CAN_L -> /INHC
- U2 pad 7: /CAN_H -> /INLC
- U2 pad 8: GND -> /NFAULT
- U4 pad 1: unconnected-(U4-OUT-Pad1) -> +5V
- U4 pad 2: unconnected-(U4-GND-Pad2) -> GND
- U4 pad 3: unconnected-(U4-~{OC}-Pad3) -> +5V
- U4 pad 5: unconnected-(U4-IN-Pad5) -> +3.3V
- U5 pad 1: +3.3V -> /CAN_TX
- U5 pad 2: /EN_GATE -> GND
- U5 pad 3: /WAKE -> +3.3V
- U5 pad 4: unconnected-(U5-PC15-Pad4) -> /CAN_RX
- U5 pad 5: /SH_B_SENSE -> unconnected-(U5-Vref-Pad5)
- U5 pad 6: /PVDDSENSE -> /CAN_L
- U5 pad 7: /NRST -> /CAN_H
- U5 pad 8: /SO1 -> GND
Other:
- copper layers 2 -> 4

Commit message: Some small changes
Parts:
- moved C1 337.6 mm to (510.1, 73.9)
- moved C10 337.6 mm to (522.8, 104.0)
- moved C11 337.6 mm to (522.8, 107.3)
- moved C12 337.6 mm to (522.8, 110.7)
- moved C13 337.6 mm to (522.8, 114.0)
- moved C14 337.6 mm to (522.8, 117.3)
- moved C2 337.6 mm to (510.1, 85.8)
- moved C21 337.6 mm to (422.4, 117.8)
- moved C22 337.6 mm to (418.5, 114.2)
- moved C23 337.6 mm to (418.5, 116.2)
- moved C24 337.6 mm to (418.5, 118.1)
- moved C25 337.6 mm to (418.5, 120.1)
- moved C26 337.6 mm to (422.4, 120.3)
- moved C27 337.6 mm to (418.5, 122.1)
- moved C28 337.6 mm to (418.5, 124.0)
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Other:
- board outline added: 100 x 50 mm

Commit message: Tentative placement of FETs in PCB
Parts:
- moved C5 431.3 mm to (80.3, 85.5)
- moved C6 431.3 mm to (80.3, 97.3)
- moved C2 430.2 mm to (80.1, 73.8)
- moved C1 430.1 mm to (80.2, 61.0)
- moved C3 429.9 mm to (80.3, 108.5)
- moved C4 429.9 mm to (80.3, 120.3)
- moved C9 370.2 mm to (154.0, 67.6), turned to 90 degrees
- moved C7 368.8 mm to (154.0, 84.7), turned to 90 degrees
- moved C11 368.5 mm to (154.2, 101.4), turned to 90 degrees
- moved C10 367.7 mm to (156.8, 67.6), turned to 90 degrees
- moved C8 366.3 mm to (156.6, 84.7), turned to 90 degrees
- moved C12 365.9 mm to (157.0, 101.4), turned to 90 degrees
- moved P1 339.5 mm to (142.9, 109.8)
- moved P2 330.3 mm to (153.0, 109.7)
- moved C13 318.5 mm to (206.1, 80.8)
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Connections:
- NT10 pad 1: /SN3 -> /SP3
- NT11 pad 1: /SP3 -> /SN3
- NT2 pad 1: /SN1 -> /SP1
- NT4 pad 1: /SP1 -> /SN1
- NT6 pad 1: /SN2 -> /SP2
- NT7 pad 1: /SP2 -> /SN2
- U1 pad 22: /NFAULT -> /DRV_NFAULT
- U2 pad 8: /NFAULT -> /DRV_NFAULT
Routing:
- net GND: track 0.00 -> 56.4 mm
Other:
- board text added: "near mcu, keep away from MOS side"
